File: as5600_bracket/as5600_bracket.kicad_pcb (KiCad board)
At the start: 2 copper layers, 42 x 42 mm, 0 parts

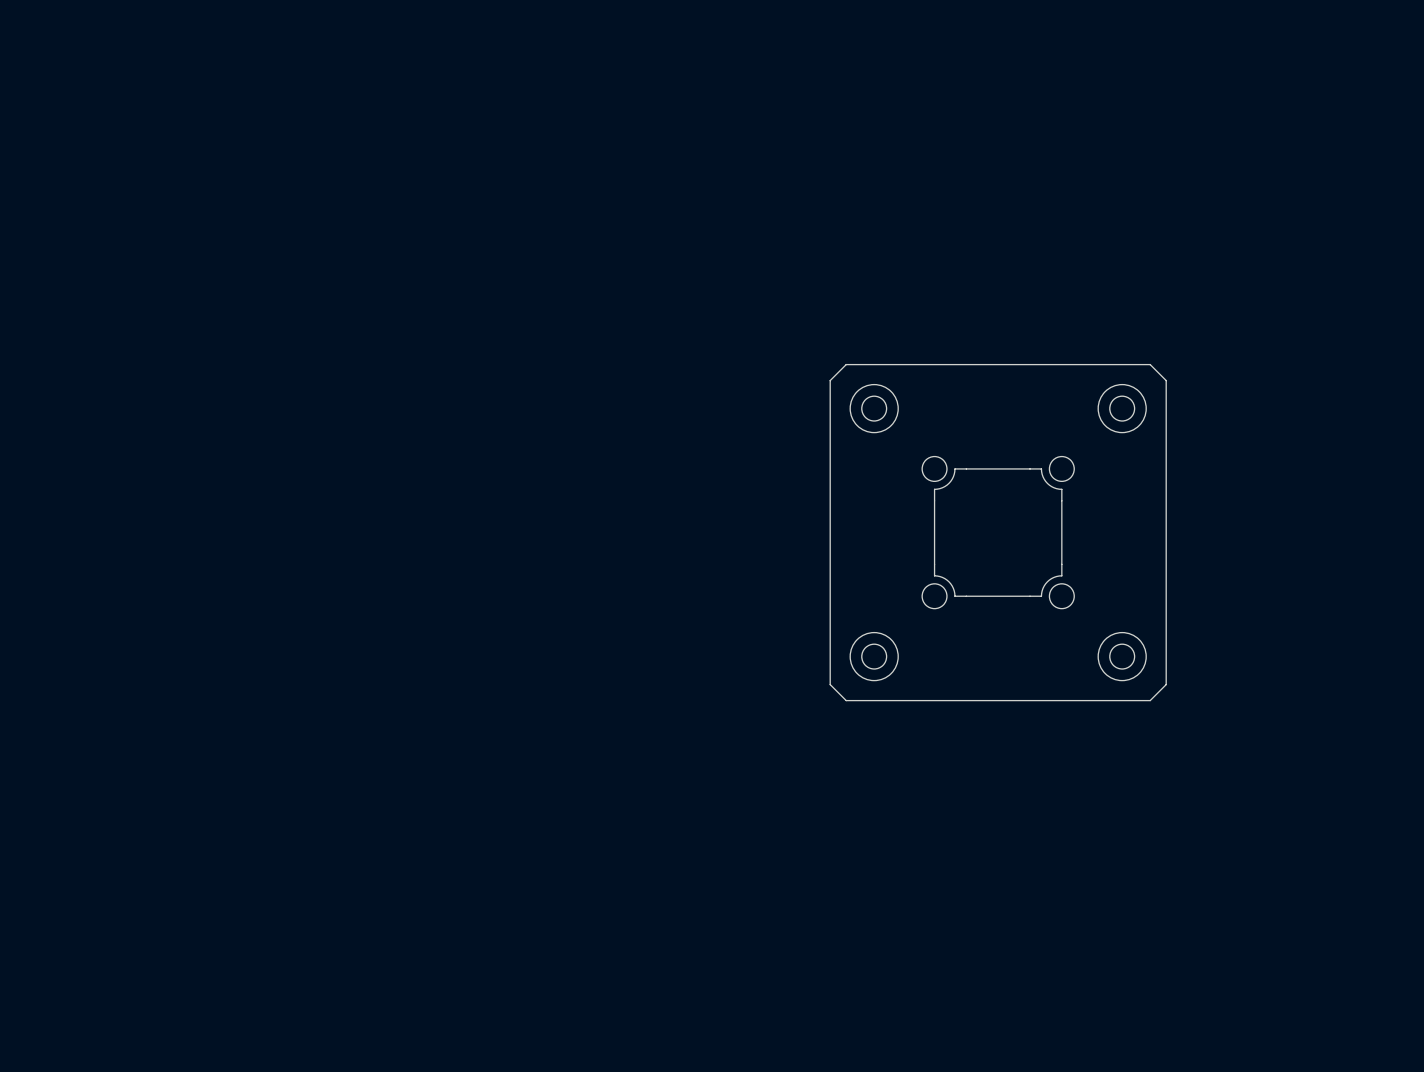
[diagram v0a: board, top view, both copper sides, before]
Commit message: done 3 variants
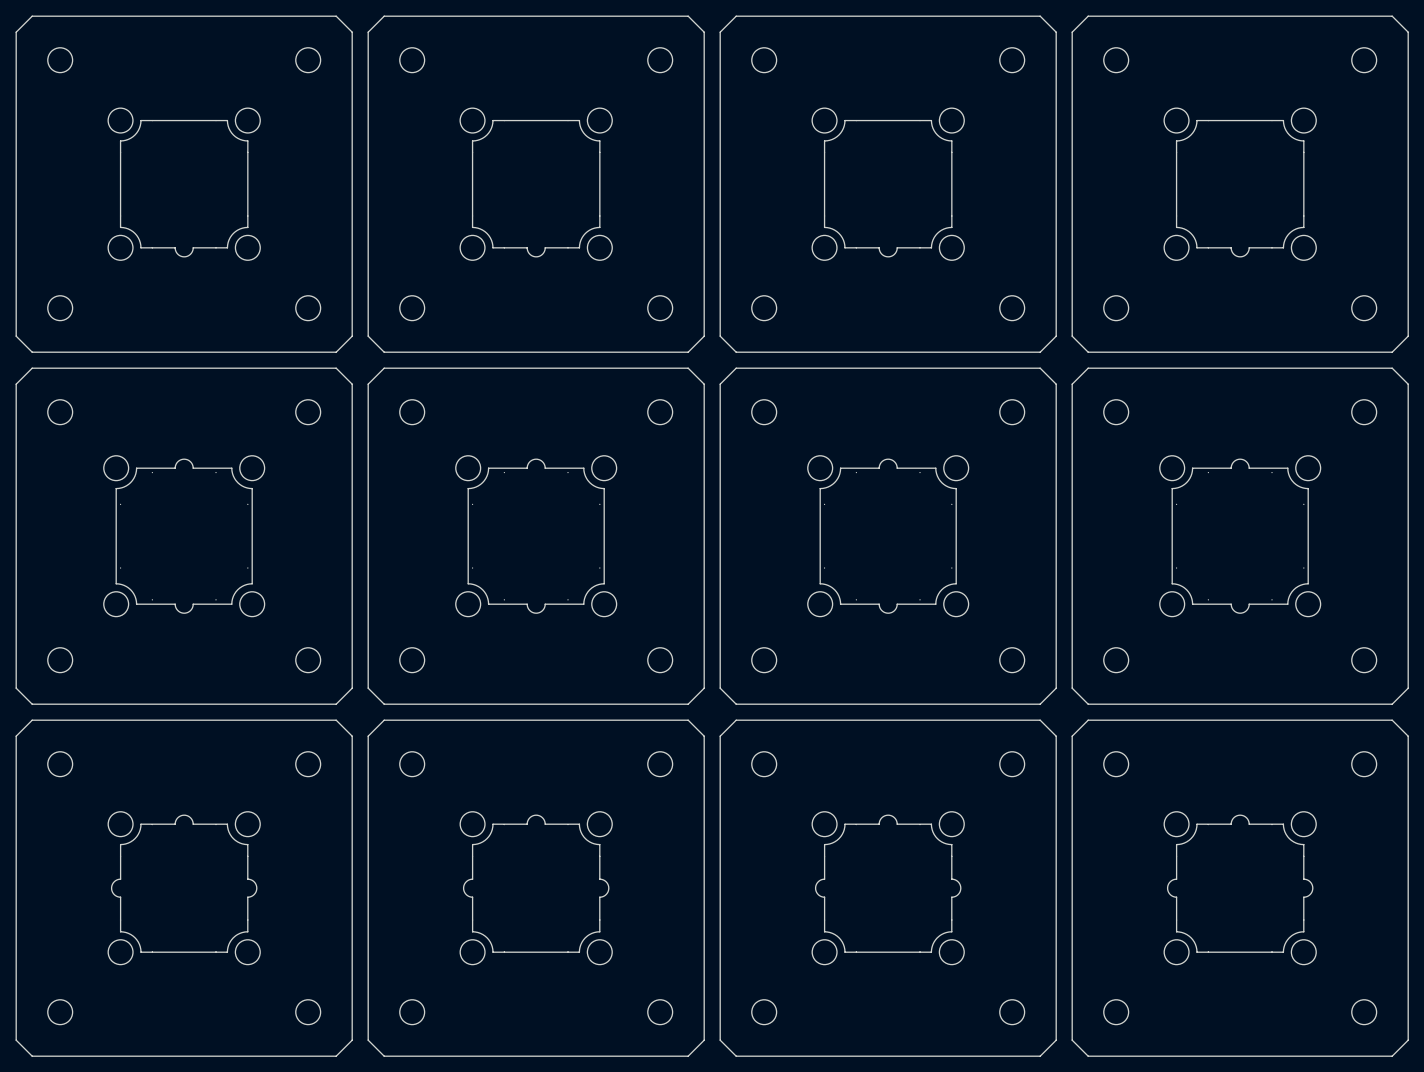
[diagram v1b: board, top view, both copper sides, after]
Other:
- board size 42 x 42 mm -> 174 x 130 mm
